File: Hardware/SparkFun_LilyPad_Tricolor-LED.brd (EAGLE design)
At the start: 20 x 20 mm, 17 parts

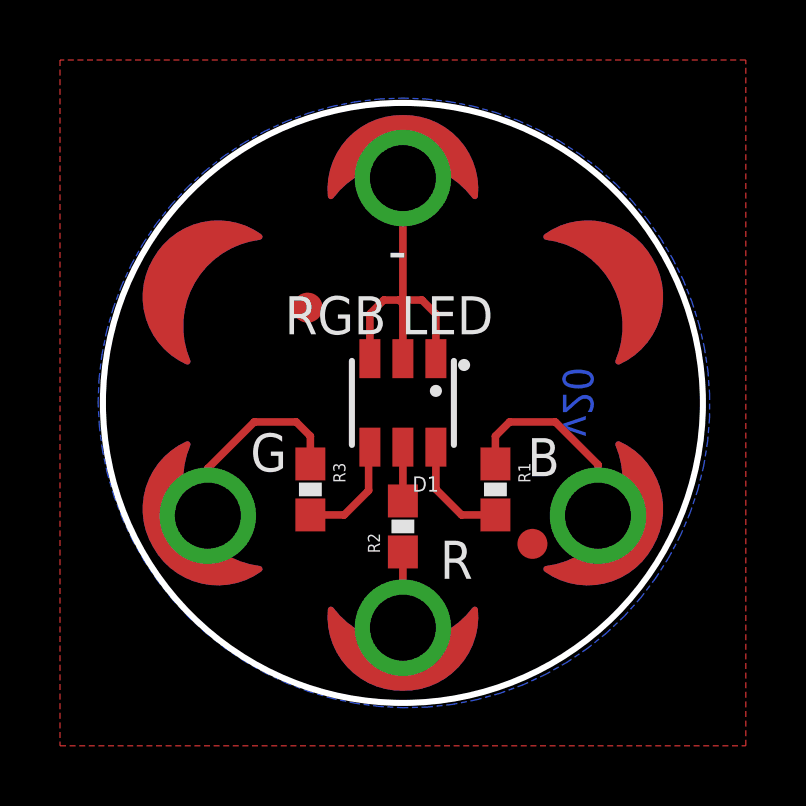
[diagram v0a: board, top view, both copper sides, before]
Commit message: Fiducial adjustment
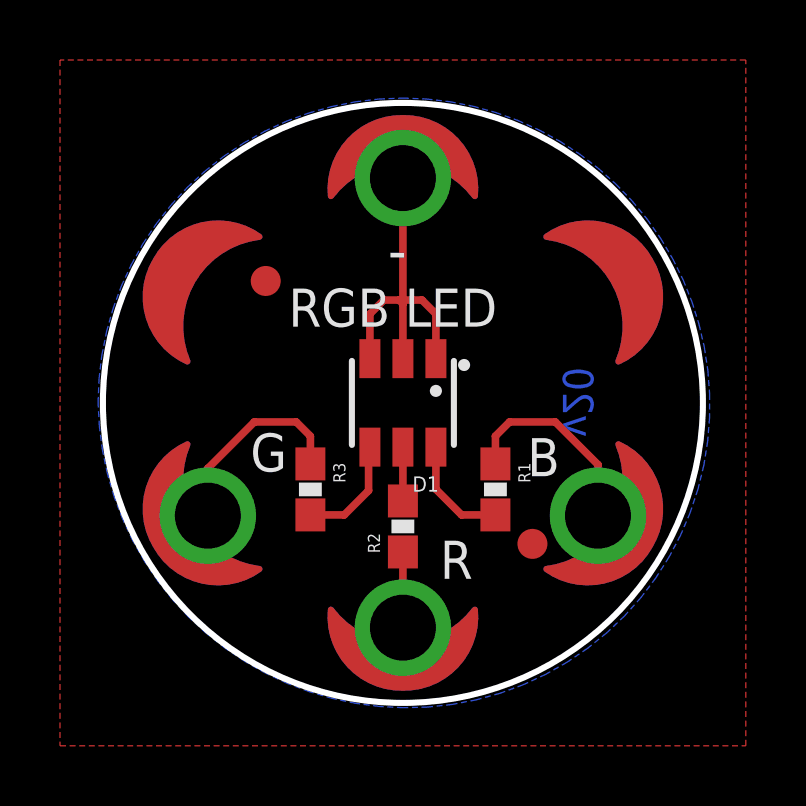
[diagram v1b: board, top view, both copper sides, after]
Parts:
- moved FID1 1.66 mm to (-4.57, 4.06)
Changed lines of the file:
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@@
 <vertex x="0" y="-8.2"/>
 </polygon>
-<text x="-3.937" y="2.286" size="1.27" layer="21" font="vector" ratio="15">RGB LED</text>
+<text x="-3.81" y="2.54" size="1.27" layer="21" font="vector" ratio="15">RGB LED</text>
 </plain>
 <attributes>
@@
 <element name="LOGO1" library="SparkFun-Aesthetics" package="OSHW-LOGO-S" value="OSHW-LOGOS" x="0" y="3.81" rot="MR0"/>
 <element name="LOGO2" library="SparkFun-Aesthetics" package="SFE_LOGO_FLAME_.1" value="SFE_LOGO_FLAME.1_INCH" x="0.889" y="-5.842" rot="MR0"/>
-<element name="FID1" library="SparkFun-Aesthetics" package="FIDUCIAL-1X2" value="FIDUCIAL1X2" x="-3.175" y="3.175"/>
+<element name="FID1" library="SparkFun-Aesthetics" package="FIDUCIAL-1X2" value="FIDUCIAL1X2" x="-4.572" y="4.064"/>
 <element name="FID2" library="SparkFun-Aesthetics" package="FIDUCIAL-1X2" value="FIDUCIAL1X2" x="4.318" y="-4.699"/>
 <element name="U$4" library="SparkFun-Aesthetics" package="REVISION" value="REVISION" x="-87.249" y="-3.048"/>

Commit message: Added extra silk *only for protos*
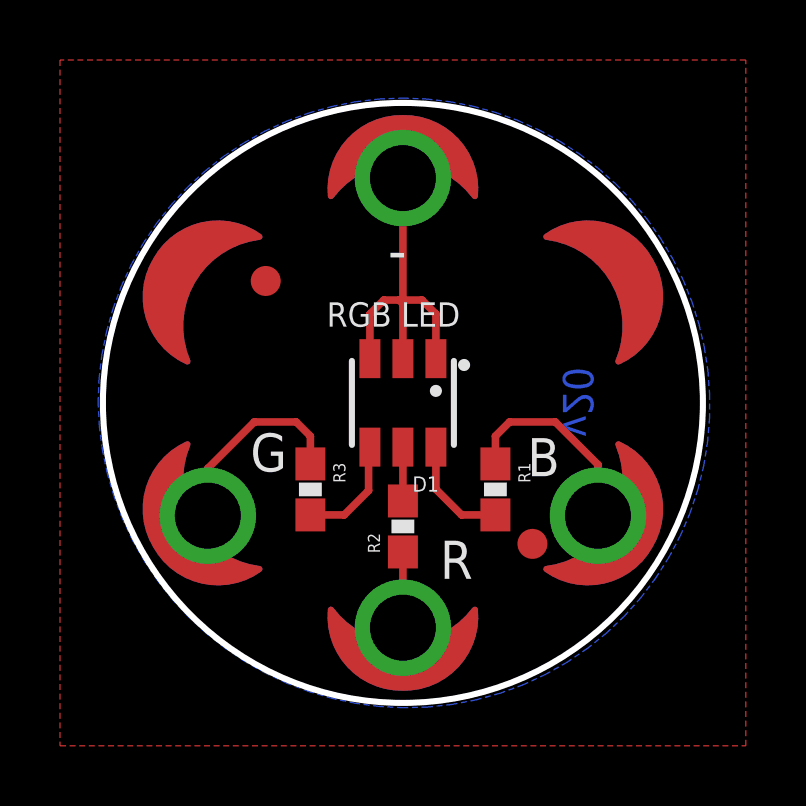
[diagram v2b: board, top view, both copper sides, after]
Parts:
- moved LOGO2 8.22 mm to (-1.02, 2.16)
- moved LOGO1 1.91 mm to (1.91, 3.68)
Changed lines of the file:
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@@
 <grid distance="0.05" unitdist="inch" unit="inch" style="lines" multiple="1" display="yes" altdistance="0.005" altunitdist="inch" altunit="inch"/>
 <layers>
-<layer number="1" name="Top" color="4" fill="1" visible="yes" active="yes"/>
+<layer number="1" name="Top" color="4" fill="1" visible="no" active="yes"/>
 <layer number="2" name="Route2" color="1" fill="3" visible="no" active="no"/>
 <layer number="3" name="Route3" color="4" fill="3" visible="no" active="no"/>
@@
 <layer number="15" name="Route15" color="4" fill="6" visible="no" active="no"/>
 <layer number="16" name="Bottom" color="1" fill="1" visible="yes" active="yes"/>
-<layer number="17" name="Pads" color="2" fill="1" visible="yes" active="yes"/>
+<layer number="17" name="Pads" color="2" fill="1" visible="no" active="yes"/>
 <layer number="18" name="Vias" color="2" fill="1" visible="yes" active="yes"/>
-<layer number="19" name="Unrouted" color="6" fill="1" visible="yes" active="yes"/>
+<layer number="19" name="Unrouted" color="6" fill="1" visible="no" active="yes"/>
 <layer number="20" name="Dimension" color="15" fill="1" visible="yes" active="yes"/>
-<layer number="21" name="tPlace" color="16" fill="1" visible="yes" active="yes"/>
+<layer number="21" name="tPlace" color="16" fill="1" visible="no" active="yes"/>
 <layer number="22" name="bPlace" color="14" fill="1" visible="yes" active="yes"/>
 <layer number="23" name="tOrigins" color="15" fill="1" visible="yes" active="yes"/>
@@
 <layer number="40" name="bKeepout" color="1" fill="11" visible="no" active="yes"/>
 <layer number="41" name="tRestrict" color="4" fill="10" visible="no" active="yes"/>
-<layer number="42" name="bRestrict" color="1" fill="10" visible="no" active="yes"/>
+<layer number="42" name="bRestrict" color="1" fill="10" visible="yes" active="yes"/>
 <layer number="43" name="vRestrict" color="2" fill="10" visible="no" active="yes"/>
 <layer number="44" name="Drills" color="7" fill="1" visible="no" active="yes"/>
@@
 <layer number="47" name="Measures" color="11" fill="1" visible="no" active="yes"/>
 <layer number="48" name="Document" color="7" fill="1" visible="no" active="yes"/>
-<layer number="49" name="Reference" color="7" fill="1" visible="yes" active="yes"/>
+<layer number="49" name="Reference" color="7" fill="1" visible="no" active="yes"/>
 <layer number="50" name="dxf" color="7" fill="1" visible="no" active="yes"/>
 <layer number="51" name="tDocu" color="6" fill="1" visible="yes" active="yes"/>
@@
 <vertex x="0" y="-8.2"/>
 </polygon>
-<text x="-3.81" y="2.54" size="1.27" layer="21" font="vector" ratio="15">RGB LED</text>
+<text x="-2.54" y="2.54" size="0.8128" layer="21" font="vector" ratio="15">RGB LED</text>
+<text x="-2.54" y="-3.81" size="0.8128" layer="22" font="vector" ratio="15" rot="MR180">RGB LED</text>
 </plain>
 <attributes>
@@
 <attribute name="DESIGNER" value="NAME" x="-98.88105625" y="0" size="1.778" layer="27" display="off"/>
 </element>
-<element name="LOGO1" library="SparkFun-Aesthetics" package="OSHW-LOGO-S" value="OSHW-LOGOS" x="0" y="3.81" rot="MR0"/>
-<element name="LOGO2" library="SparkFun-Aesthetics" package="SFE_LOGO_FLAME_.1" value="SFE_LOGO_FLAME.1_INCH" x="0.889" y="-5.842" rot="MR0"/>
+<element name="LOGO1" library="SparkFun-Aesthetics" package="OSHW-LOGO-S" value="OSHW-LOGOS" x="1.905" y="3.683" rot="MR0"/>
+<element name="LOGO2" library="SparkFun-Aesthetics" package="SFE_LOGO_FLAME_.1" value="SFE_LOGO_FLAME.1_INCH" x="-1.016" y="2.159" rot="MR0"/>
 <element name="FID1" library="SparkFun-Aesthetics" package="FIDUCIAL-1X2" value="FIDUCIAL1X2" x="-4.572" y="4.064"/>
 <element name="FID2" library="SparkFun-Aesthetics" package="FIDUCIAL-1X2" value="FIDUCIAL1X2" x="4.318" y="-4.699"/>
